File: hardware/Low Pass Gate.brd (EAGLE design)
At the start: 40.6 x 101.6 mm, 99 parts, among them IC1 TL072, IC2 LM397, IC3 TL072, IC4 TL072, IC5 LM397, IC6 TL072, P1 POWER_SIMPLE10_SHROUDED, Q1 112, Q2 112

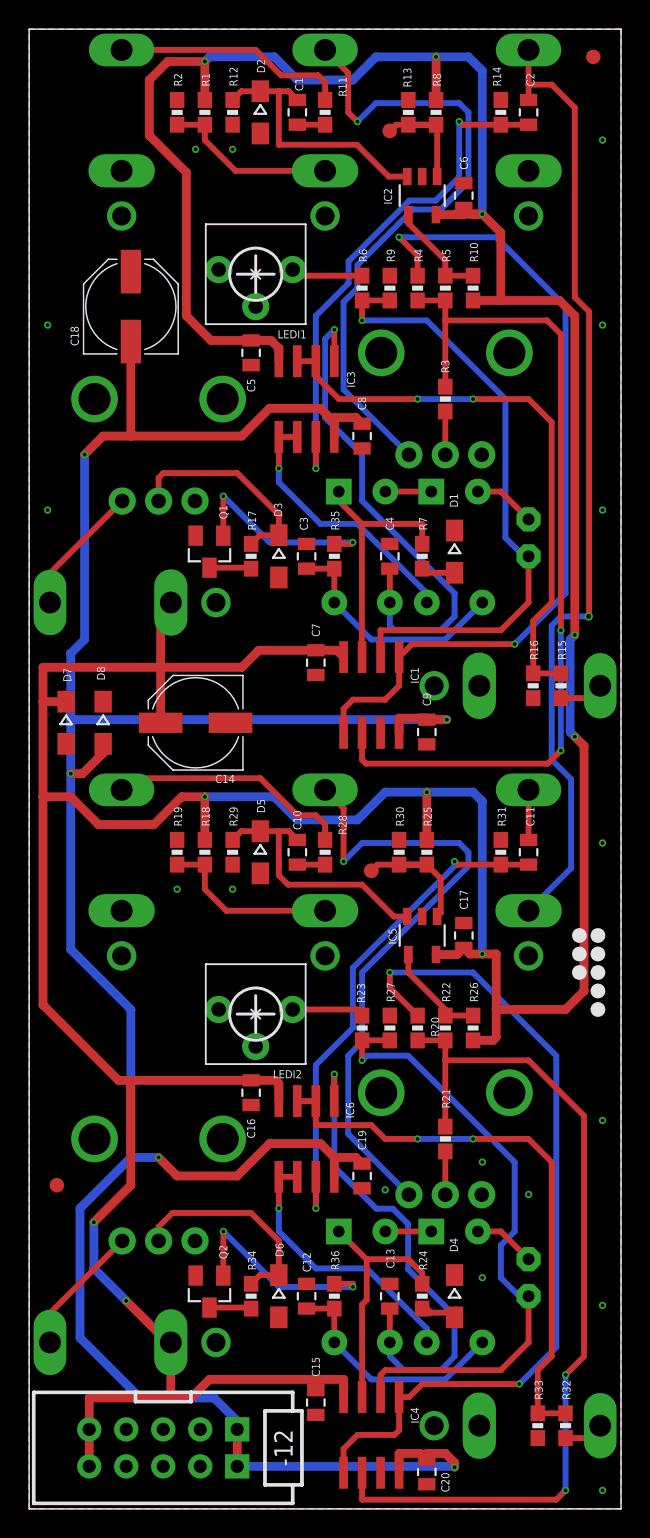
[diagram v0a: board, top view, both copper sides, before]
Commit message: add test fixture alignment holes
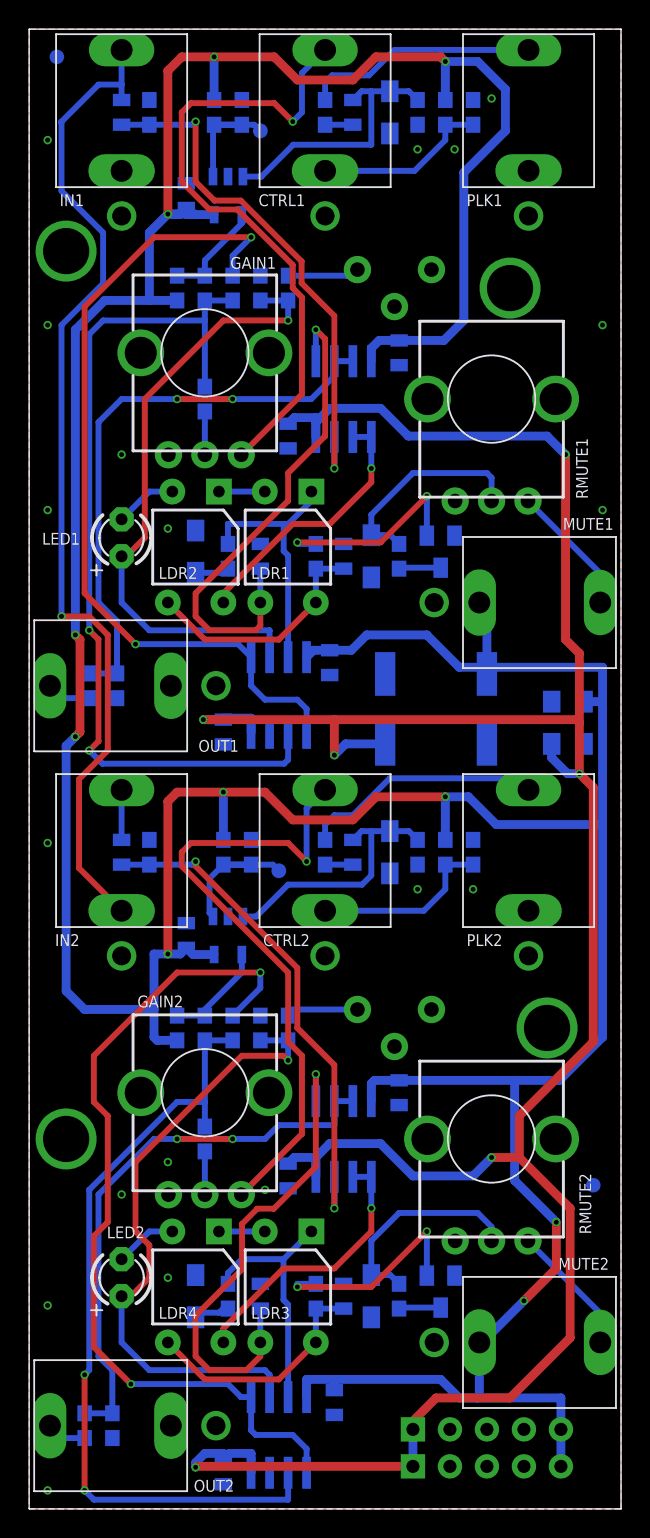
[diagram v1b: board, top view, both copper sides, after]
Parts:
- moved U$1 36.8 mm to (38.7, 22.2), flipped to the bottom
- moved U$2 36.8 mm to (1.91, 99.7), flipped to the bottom
- moved D7 35.6 mm to (38.1, 54.0), flipped to the bottom
- moved R32 33.0 mm to (3.81, 5.71), flipped to the bottom
- moved C18 32.7 mm to (24.4, 54.9), flipped to the bottom
- moved R15 32.4 mm to (4.13, 56.5), flipped to the bottom
- moved D8 30.8 mm to (35.9, 54.0), flipped to the bottom
- moved R33 29.2 mm to (5.71, 5.71), flipped to the bottom
- moved R16 28.6 mm to (6.03, 56.5), flipped to the bottom
- moved C11 27.9 mm to (6.35, 45.1), flipped to the bottom
- moved C2 27.9 mm to (6.35, 95.9), flipped to the bottom
- moved IN1 27.9 mm to (6.35, 95.2), flipped to the top
- moved IN2 27.9 mm to (6.35, 44.5), flipped to the top
- moved LED1 27.9 mm to (6.35, 66.7), flipped to the top
- moved LED2 27.9 mm to (6.35, 15.9), flipped to the top
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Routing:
- net N$1: track 61.2 -> 55.1 mm
- net +12V: track 325.7 -> 322.0 mm
- net IN-1: track 66.7 -> 69.6 mm
- net N$28: track 39.7 -> 38.4 mm
- net VSIG: track 58.0 -> 58.8 mm
- net N$18: track 60.7 -> 61.2 mm
- net -12V: track 183.3 -> 183.7 mm, vias 5 -> 6
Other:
- board text added: "2019.06.22"
- board text removed: "2018.06.15"

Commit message: use throughhole bulk caps
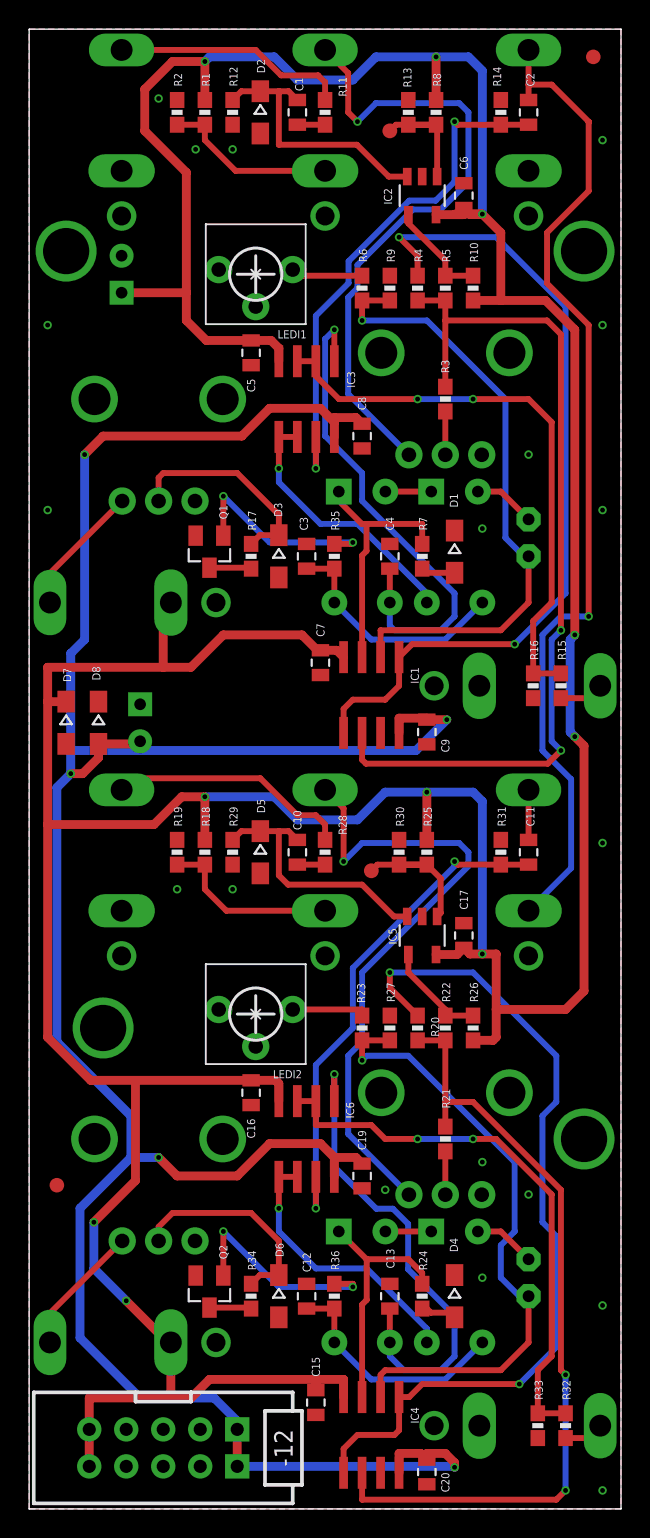
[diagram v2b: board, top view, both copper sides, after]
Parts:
- removed C14, C18: 100u, SparkFun-Passives:PANASONIC_D
- added C21, C22: 100u, SparkFun-Passives:CPOL-RADIAL-100UF-25V
- moved U$1 36.8 mm to (1.91, 22.2), flipped to the top
- moved U$2 36.8 mm to (38.7, 99.7), flipped to the top
- moved D7 35.6 mm to (2.54, 54.0), flipped to the top
- moved R32 33.0 mm to (36.8, 5.71), flipped to the top
- moved R15 32.4 mm to (36.5, 56.5), flipped to the top
- moved D8 31.1 mm to (4.76, 54.0), flipped to the top
- moved R33 29.2 mm to (34.9, 5.71), flipped to the top
- moved R16 28.6 mm to (34.6, 56.5), flipped to the top
- moved C11 27.9 mm to (34.3, 45.1), flipped to the top
- moved C2 27.9 mm to (34.3, 95.9), flipped to the top
- moved IN1 27.9 mm to (34.3, 95.2), flipped to the bottom
- moved IN2 27.9 mm to (34.3, 44.5), flipped to the bottom
- moved LED1 27.9 mm to (34.3, 66.7), flipped to the bottom
- moved LED2 27.9 mm to (34.3, 15.9), flipped to the bottom
- moved MUTE1 27.9 mm to (6.35, 62.2), flipped to the bottom
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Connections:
- net +12V: now also C21.1; no longer C14.+
- net -12V: now also C22.2; no longer C18.-
- net GND: now also C21.2, C22.1; no longer C14.-, C18.+
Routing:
- net +12V: track 322.0 -> 325.8 mm
- net -12V: track 183.7 -> 181.2 mm, vias 6 -> 5

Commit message: fix power connector location for keyed connector width
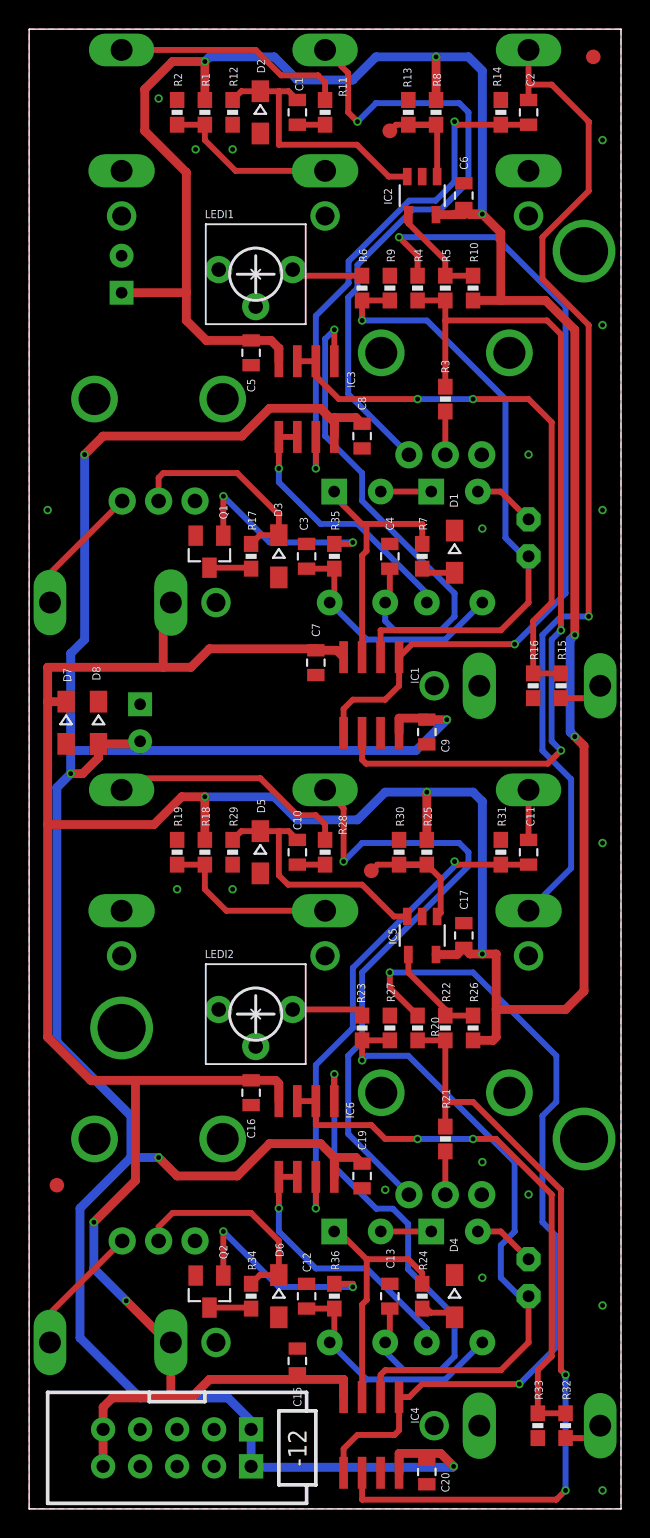
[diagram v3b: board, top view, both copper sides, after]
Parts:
- moved C15 3.13 mm to (18.4, 10.2), turned to 90 degrees
- moved P1 0.95 mm to (10.2, 4.19)
- moved C7 0.32 mm to (19.7, 58.1)
- moved LDR1 0.32 mm to (22.5, 66.0)
- moved LDR3 0.32 mm to (22.5, 15.2)
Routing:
- net +12V: track 325.8 -> 323.5 mm
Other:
- board text added: "INTERNATIONAL KNITTING"
- board text added: "LOW PASS GATE revH"
- board text removed: "INTERNATION KNITTING"
- board text removed: "LOW PASS GATE REV H"

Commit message: revert to using ldr muting circuit
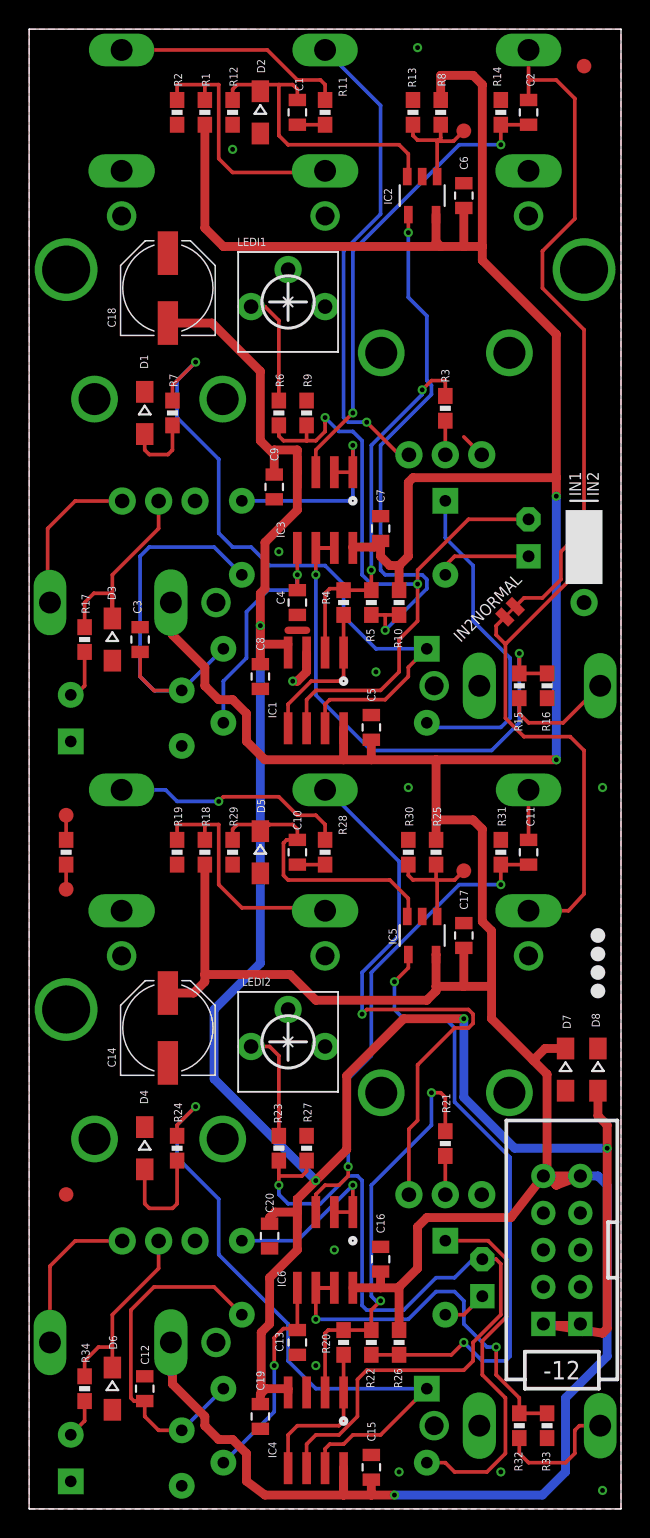
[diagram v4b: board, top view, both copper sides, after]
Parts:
- removed C21, C22: 100u, SparkFun-Passives:CPOL-RADIAL-100UF-25V
- removed Q1, Q2: 112, barsstronics:SOT23-3
- removed R35, R36: 0R, SparkFun-Passives:0603-RES
- added C14, C18: 100u, SparkFun-Passives:PANASONIC_D
- added IN2NORMAL: (no value), SparkFun-Passives:PAD-JUMPER-2-NC_BY_TRACE_NO_SILK
- added JP1: (no value), SparkFun-Connectors:1X03_NO_SILK
- added LDR5: VTL5CVACTROL-SMALL, optocoupler:VTL5C
- added LDR6: VTL5C9, optocoupler:VTL5C-SMALL
- added RA1: OPEN, SparkFun-Passives:0603-RES
- added TP1, TP2: TEST-POINT3X4, SparkFun-Passives:PAD.03X.04
- C13, C4: value 1n -> 100p
- LDR1, LDR2, LDR4: value VTL5C9SMALL -> VTL5CVACTROL-SMALL; device optocoupler:VTL5C-SMALL -> optocoupler:VTL5C
- LDR3: value VTL5C9SMALL -> VTL5C9
- moved LDR3 42.2 mm to (6.67, 54.3), turned to 180 degrees
- moved D7 41.7 mm to (36.8, 30.2)
- moved D8 41.7 mm to (39.1, 30.2)
- moved P1 29.7 mm to (36.6, 17.8), turned to 90 degrees
- moved C5 27.0 mm to (23.5, 53.7), turned to 90 degrees
- moved D4 23.6 mm to (7.94, 24.8)
- moved D1 23.3 mm to (7.94, 75.2)
- moved R20 22.2 mm to (21.6, 11.4), turned to 90 degrees
- moved R22 22.2 mm to (23.5, 11.4), turned to 270 degrees
- moved R26 22.2 mm to (25.4, 11.4), turned to 270 degrees
- moved R10 22.2 mm to (25.4, 62.2), turned to 270 degrees
- moved R4 22.2 mm to (21.6, 62.2), turned to 90 degrees
- moved R5 22.2 mm to (23.5, 62.2), turned to 270 degrees
- moved C9 19.8 mm to (16.8, 70.2)
- moved R7 19.8 mm to (9.84, 75.2)
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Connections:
- removed net N$38: Q1.1, R35.2
- removed net N$52: Q2.1, R36.2
- new net N$36: RA1.2, TP2.P$1
- new net N$4: RA1.1, TP1.P$1
- new net N$55: IN2.N, IN2NORMAL.1, JP1.2
- net +12V: now also C14.+; no longer C21.1
- net -12V: now also C18.-; no longer C22.2
- net GND: now also C14.-, C18.+, JP1.1, LDR3.1, LDR3.3, LDR6.1, LDR6.3; no longer C21.2, C22.1, Q1.2, Q2.2
- net IN-1: now also IN2NORMAL.2, JP1.3; no longer IN2.N
- net N$2: now also LDR4.1; no longer LDR3.1
- net N$25: now also LDR4.4; no longer LDR3.4
- net N$27: now also LDR5.3; no longer LDR4.3
- net N$3: now also LDR4.2, LDR5.1; no longer LDR3.2, LDR4.1
- net N$30: now also LDR6.2; no longer Q2.3
- net N$31: now also LDR4.3, LDR5.4, LDR6.4; no longer LDR3.3, LDR4.4, R36.1
- net N$44: now also LDR3.4; no longer R35.1
- net N$46: now also LDR3.2; no longer Q1.3
- net N$7: now also LDR5.2; no longer LDR4.2
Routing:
- net VSIG: track 58.8 -> 11.0 mm, vias 2 -> 0
- net VSIG1: track 57.6 -> 10.5 mm, vias 2 -> 0
- net N$14: track 7.15 -> 43.5 mm, vias 0 -> 2
- net N$18: track 61.2 -> 25.5 mm
- net N$55: track 0.00 -> 35.6 mm
- net N$21: track 7.15 -> 37.6 mm, vias 0 -> 2
- net N$48: track 17.8 -> 46.2 mm, vias 0 -> 1
- net N$2: track 17.6 -> 44.0 mm, vias 0 -> 1
- net N$1: track 55.1 -> 29.5 mm
- net -12V: track 181.3 -> 158.1 mm, vias 5 -> 4
- net IN-1: track 69.9 -> 46.8 mm, vias 1 -> 0
- net N$3: track 3.47 -> 25.6 mm
- net N$49: track 3.47 -> 22.9 mm
- net N$25: track 34.1 -> 14.8 mm
- net N$41: track 34.9 -> 16.3 mm
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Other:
- board text added: "2017.09.09"
- board text added: "IN1 IN2"
- board text added: "LPG rev D"
- board text added: "US KNITTING"
- board text removed: "2019.06.22"
- board text removed: "INTERNATIONAL KNITTING"
- board text removed: "LOW PASS GATE revH"

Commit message: update to rev E
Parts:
- removed C17, C20, C7, C9: 100n, SparkFun-Passives:0805
- removed IC1, IC3, IC4, IC6: TL072, linear:SO08
- removed IN2NORMAL: (no value), SparkFun-Passives:PAD-JUMPER-2-NC_BY_TRACE_NO_SILK
- removed JP1: (no value), SparkFun-Connectors:1X03_NO_SILK
- removed LEDI1, LEDI2: 5K, SparkFun-Electromechanical:TRIM_POT
- removed R23, R6: 500R (opt), SparkFun-Passives:0603-RES
- removed RA1: OPEN, SparkFun-Passives:0603-RES
- removed TP1, TP2, TRIGGERREF1, TRIGGERREF2: TEST-POINT3X4, SparkFun-Passives:PAD.03X.04
- added C21, C22: 560p, SparkFun-Passives:0805
- added U1, U2: OPAMP-QUADSO14, barsstronics:SO14
- CTRL1, CTRL2, IN1, IN2: value AUDIO-JACKINLINE -> AUDIO-JACKINLINE-FLOATGND; device erthenvar:ERTHENVAR-JACK-INLINE -> erthenvar:ERTHENVAR-JACK-INLINE-SHAREGND550
- LDR1, LDR2, LDR4, LDR5: value VTL5CVACTROL-SMALL -> VTL5C9SMALL; device optocoupler:VTL5C -> optocoupler:VTL5C-SMALL
- LDR3, LDR6: value VTL5C9 -> VTL5C9SMALL
- moved P1 75.0 mm to (11.1, 88.3), turned to 180 degrees
- moved D7 58.7 mm to (28.3, 88.3)
- moved D8 58.7 mm to (30.5, 88.3)
- moved C18 49.4 mm to (26.7, 37.5), turned to 180 degrees
- moved U$1 38.1 mm to (35.6, 2.54)
- moved U$2 33.0 mm to (5.08, 97.8)
- moved IC2 22.4 mm to (14.3, 71.8)
- moved IC5 22.4 mm to (14.3, 21.0)
- moved C6 22.2 mm to (17.5, 71.8)
- moved C2 21.6 mm to (19.7, 80.0)
- moved R14 21.6 mm to (17.8, 80.0)
- moved C11 21.4 mm to (20.0, 29.2)
- moved R31 21.4 mm to (18.1, 29.2)
- moved R13 20.1 mm to (14.0, 80.0)
- moved R8 20.1 mm to (15.9, 80.0)
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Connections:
- removed net N$19: LEDI2.2, R23.1
- removed net N$36: RA1.2, TP2.P$1
- removed net N$37: LEDI1.2, R6.1
- removed net N$4: RA1.1, TP1.P$1
- removed net N$55: IN2.N, IN2NORMAL.1, JP1.2
- net +12V: now also U1.4, U2.4; no longer C17.1, C7.1, IC1.8, IC3.8, IC4.8, IC6.8
- net -12V: now also U1.11, U2.11; no longer C20.2, C9.2, IC1.4, IC3.4, IC4.4, IC6.4
- net GND: now also U1.12, U2.12; no longer C17.2, C20.1, C7.2, C9.1, IC1.3, IC4.3, JP1.1, LEDI1.1, LEDI1.3, LEDI2.1, LEDI2.3
- net IN-1: now also IN2.N; no longer IN2NORMAL.2, JP1.3
- net N$1: now also U2.13; no longer IC4.2
- net N$17: no longer TRIGGERREF2.P$1
- net N$18: now also U1.13; no longer IC1.2
- net N$2: now also U2.8; no longer IC4.7
- net N$24: now also U2.3; no longer IC6.3
- net N$25: now also U2.5; no longer IC6.5
- net N$27: now also U2.1, U2.2; no longer IC6.1, IC6.2
- net N$28: now also C22.1, U2.6, U2.7; no longer IC6.6, IC6.7
- net N$31: now also C22.2
- net N$32: no longer TRIGGERREF1.P$1
- net N$40: now also U1.3; no longer IC3.3
- net N$41: now also U1.5; no longer IC3.5
- net N$42: now also U1.1, U1.2; no longer IC3.1, IC3.2
- net N$43: now also C21.1, U1.6, U1.7; no longer IC3.6, IC3.7
- net N$44: now also C21.2
- net N$48: now also U1.8; no longer IC1.7
- net N$53: now also U1.9; no longer IC1.6, R6.2
- net N$6: now also U2.9; no longer IC4.6, R23.2
- net VSIG: now also U2.10, U2.14; no longer IC4.1, IC4.5
- net VSIG1: now also U1.10, U1.14; no longer IC1.1, IC1.5
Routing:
- net +12V: track 309.5 -> 213.9 mm, vias 3 -> 6
- net N$55: track 35.6 -> 0.00 mm
- net N$6: track 56.2 -> 22.4 mm, vias 1 -> 0
- net IN-1: track 46.8 -> 79.3 mm, vias 0 -> 3
- net N$31: track 24.2 -> 53.4 mm, vias 0 -> 1
- net N$53: track 49.5 -> 22.6 mm, vias 2 -> 0
- net N$48: track 46.2 -> 20.5 mm, vias 1 -> 0
- net N$44: track 28.5 -> 53.0 mm, vias 0 -> 1
- net N$2: track 44.0 -> 20.5 mm, vias 1 -> 0
- net N$13: track 3.44 -> 26.1 mm, vias 0 -> 1
- net N$18: track 25.5 -> 43.5 mm
- net N$8: track 17.1 -> 33.7 mm, vias 0 -> 1
- net N$14: track 43.5 -> 27.2 mm
- net N$3: track 25.6 -> 9.89 mm
- net N$20: track 17.8 -> 32.6 mm, vias 0 -> 1
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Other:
- board size 40.6 x 101.6 mm -> 40.6 x 100 mm
- board text added: "2019.07.18"
- board text added: "INTERNATIONAL KNITTING"
- board text added: "LPG rev E"
- board text removed: "2017.09.09"
- board text removed: "IN1 IN2"
- board text removed: "LPG rev D"
- board text removed: "US KNITTING"

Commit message: updated BOM for rev E
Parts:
- C12, C3: value 91p -> 100p
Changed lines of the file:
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@@
 <attribute name="VALUE" x="11.2395" y="31.0515" size="0.4064" layer="27" font="vector" ratio="13" rot="R90" align="center-left"/>
 </element>
-<element name="C12" library="SparkFun-Passives" package="0805" value="91p" x="15.24" y="13.335" smashed="yes" rot="R90">
+<element name="C12" library="SparkFun-Passives" package="0805" value="100p" x="15.24" y="13.335" smashed="yes" rot="R90">
 <attribute name="NAME" x="15.2527" y="14.986" size="0.5588" layer="25" font="vector" ratio="13" rot="R90" align="center-left"/>
 <attribute name="VALUE" x="15.8877" y="14.9733" size="0.4064" layer="27" font="vector" ratio="13" rot="R90" align="center-left"/>
@@
 <attribute name="VALUE" x="20.447" y="81.8515" size="0.4064" layer="27" font="vector" ratio="13" rot="R90" align="center-left"/>
 </element>
-<element name="C3" library="SparkFun-Passives" package="0805" value="91p" x="14.9225" y="64.135" smashed="yes" rot="R90">
+<element name="C3" library="SparkFun-Passives" package="0805" value="100p" x="14.9225" y="64.135" smashed="yes" rot="R90">
 <attribute name="NAME" x="14.9225" y="65.913" size="0.5588" layer="25" font="vector" ratio="13" rot="R90" align="center-left"/>
 <attribute name="VALUE" x="15.6845" y="65.9765" size="0.4064" layer="27" font="vector" ratio="13" rot="R90" align="center-left"/>
